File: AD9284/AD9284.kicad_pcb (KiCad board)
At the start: 4 copper layers, 72.2 x 72.2 mm, 108 parts, among them J10 Conn_01x01_Pin, J11 Conn_Coaxial, J12 Conn_Coaxial, J13 Conn_Coaxial, J14 Conn_Coaxial, J15 Conn_01x01_Pin, J16 Conn_01x01_Pin, J17 Conn_01x01_Pin, J18 Conn_01x01_Pin, J19 Conn_01x01_Pin, J2 Conn_01x01_Pin, J20 Conn_01x01_Pin, J21 Conn_01x01_Pin, J22 Conn_01x01_Pin, J23 Conn_01x01_Pin, J24 Conn_01x01_Pin, J25 Conn_01x01_Pin, J26 Conn_01x01_Pin, J3 Conn_01x01_Pin, J4 Conn_01x01_Pin, J5 Conn_01x01_Pin, J6 Conn_01x01_Pin, J7 Conn_01x01_Pin, J8 Conn_01x01_Pin, J9 Conn_01x01_Pin, U1 PPPC062LJBN-RC, U10 DS90LV048ATMX/NOPB, U11 DS90LV048ATMX/NOPB, U12 DS90LV011ATMF/NOPB, U13 AD8052ARMZ-REEL7, U14 AD8052ARMZ-REEL7, U2 PPPC062LJBN-RC, U3 AD9284BCPZ-250, U4 TLV70018DCKR, U5 TLV70018DCKR, U6 TXB0101DBVR, U7 TXB0101DBVR, U8 TXB0101DBVR, U9 DS90LV048ATMX/NOPB

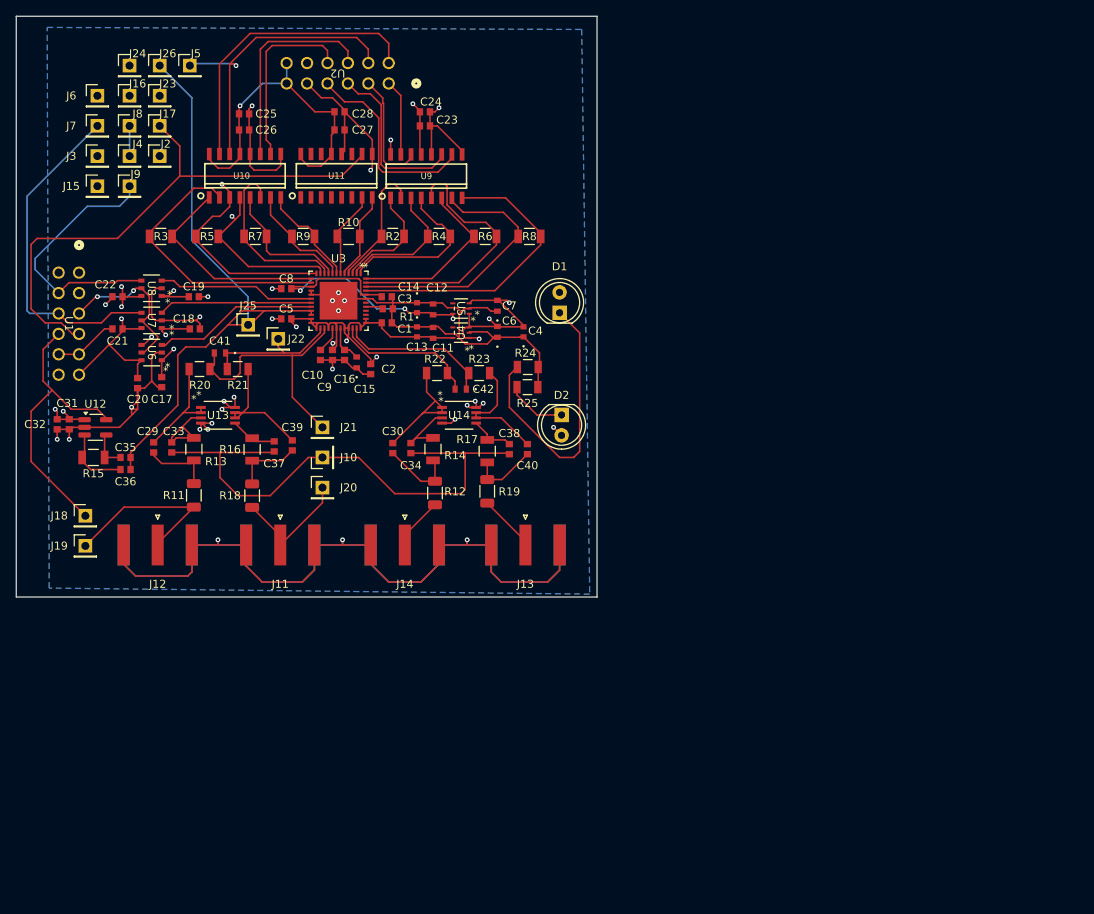
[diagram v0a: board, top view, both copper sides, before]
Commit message: Schematic and PCB complete. TODO: BOM
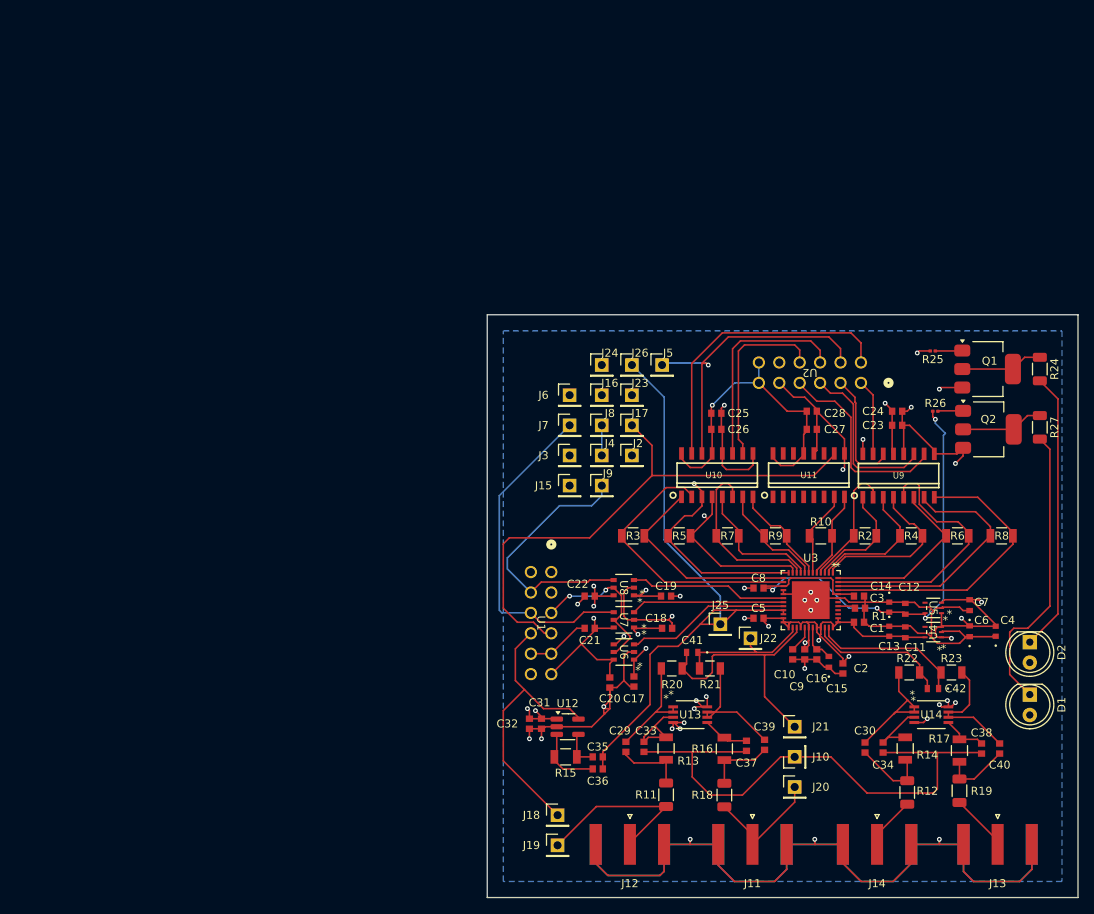
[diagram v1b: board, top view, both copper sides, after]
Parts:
- added Q1: PZT3904T1G, Package_TO_SOT_SMD:SOT-223-3_TabPin2, F.Cu at (172.0, 67.0)
- added Q2: PZT3904T1G, Package_TO_SOT_SMD:SOT-223-3_TabPin2, F.Cu at (172.1, 74.5)
- added R26: CRGP0603F47K, Resistor_SMD:R_0201_0603Metric, F.Cu at (165.5, 72.2)
- added R27: CRCW120675R0FKEAHP, Resistor_SMD:R_1206_3216Metric, F.Cu at (178.5, 74.2)
- C11, C12: value CAP_GCM188_MUR -> GCM188R71E105KA64D
- C13, C14: value G-188_MUR -> GRM188R60J106ME47D
- D1, D2: value LED -> 5219320F
- R10, R15, R2, R3, R4, R5, R6, R7, R8, R9: value RES_RMCF1206_STP -> RMCF1206FG100R
- R24: value R_US -> CRCW120675R0FKEAHP; footprint part_library:RC1206FR_0733RL -> Resistor_SMD:R_1206_3216Metric
- R25: value R_US -> CRGP0603F47K; footprint part_library:RC1206FR_0733RL -> Resistor_SMD:R_0201_0603Metric
- moved D1 75.4 mm to (177.2, 107.5), turned to -90 degrees
- moved C18 69.6 mm to (132.1, 99.2)
- moved C27 69.6 mm to (150.1, 74.5)
- moved C28 69.6 mm to (150.1, 72.2)
- moved R1 69.6 mm to (156.1, 96.8)
- moved R9 69.6 mm to (145.6, 87.8)
- moved U10 69.6 mm to (138.4, 80.2)
- moved U2 69.6 mm to (156.2, 68.7)
- moved C1 69.6 mm to (156.0, 98.5)
- moved C10 69.6 mm to (147.8, 102.5)
- moved C15 69.6 mm to (152.2, 103.4)
- moved C16 69.6 mm to (150.8, 102.5)
- moved C17 69.6 mm to (128.0, 105.9)
- moved C19 69.6 mm to (132.0, 95.2)
- moved C2 69.6 mm to (154.0, 104.2)
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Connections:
- D1 pad 2: VCC_Analog_1v8 -> VCC_3v3
- D2 pad 2: VCC_Digital_1v8 -> VCC_3v3
- R24 pad 1: Net-(D1-K) -> Net-(Q1-C)
- R24 pad 2: GND -> Net-(D2-K)
- R25 pad 1: Net-(D2-K) -> Net-(Q1-B)
- R25 pad 2: GND -> VCC_Analog_1v8
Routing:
- net Net-(D2-K): track 7.55 -> 34.9 mm
- net Net-(Q2-C): track 0.00 -> 10.3 mm
- net Net-(Q1-C): track 0.00 -> 10.3 mm
- net VCC_Digital_1v8: track 87.1 -> 94.5 mm
- net Net-(Q1-B): track 0.00 -> 3.37 mm
- net Net-(Q2-B): track 0.00 -> 3.15 mm
- net GND: track 334.3 -> 336.6 mm, vias 23 -> 25
- net VCC_Analog_1v8: track 54.8 -> 56.5 mm, vias 7 -> 8
- net Net-(D1-K): track 35.3 -> 36.4 mm
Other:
- board size 72.2 x 72.2 mm -> 73.5 x 72.5 mm
